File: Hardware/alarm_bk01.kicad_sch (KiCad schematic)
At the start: 18 parts, among them Q1 2N3904, SW1 START, SW2 Sensor, SW3 SW_SPDT, U1 ATtiny85V-10P

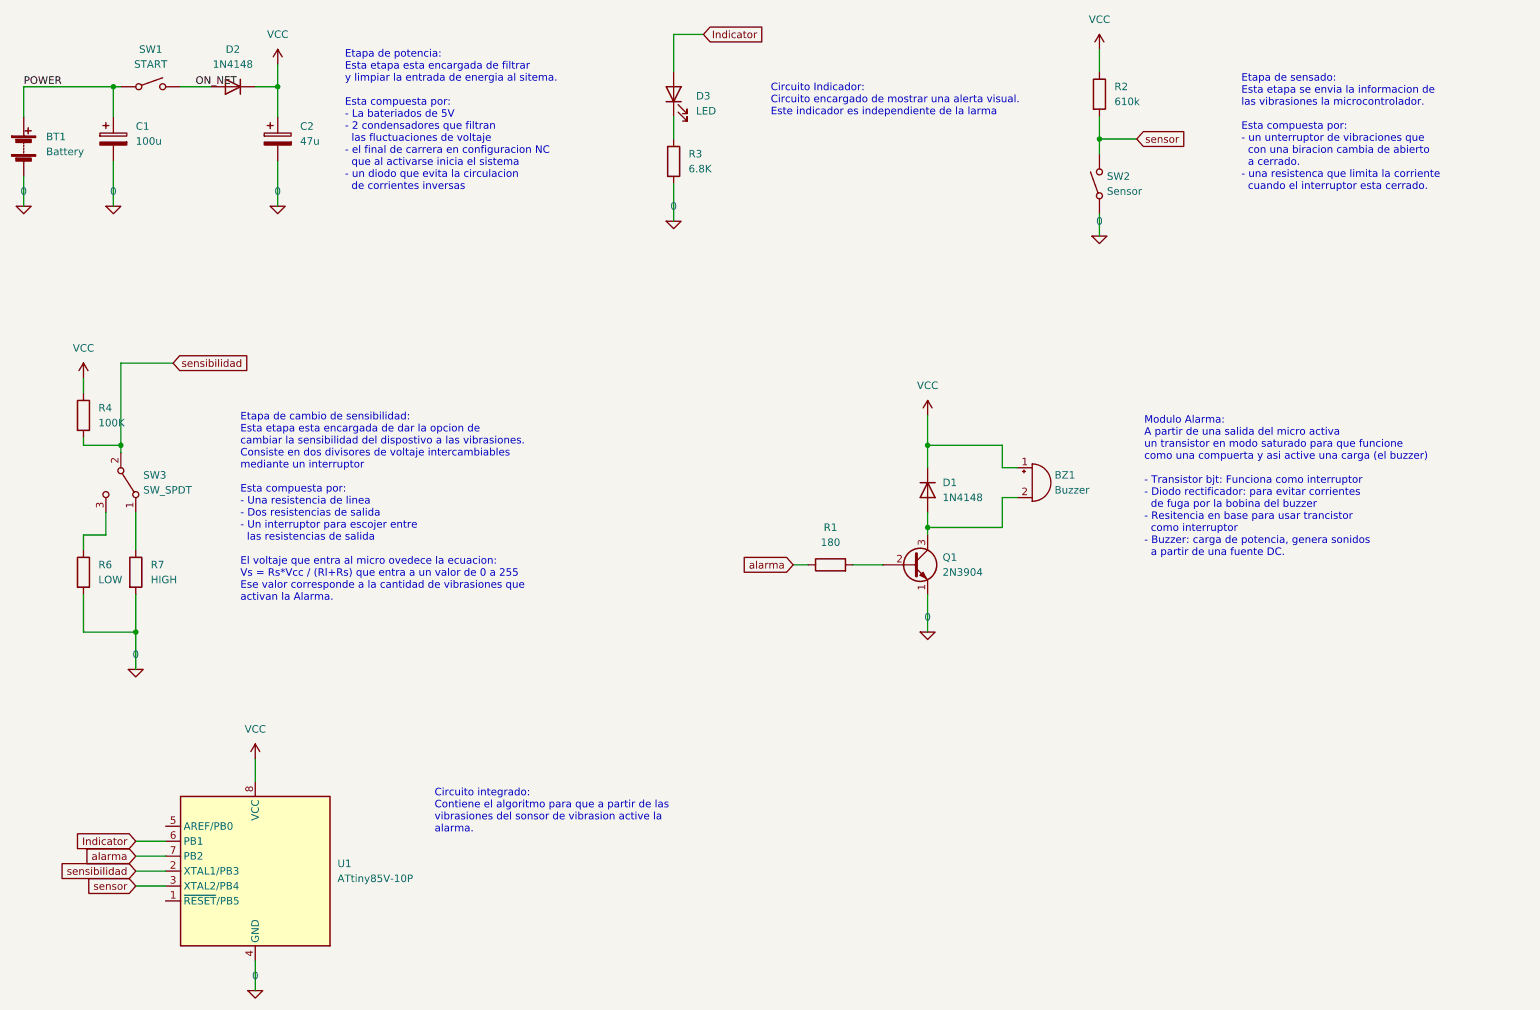
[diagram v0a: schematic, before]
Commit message: add smd design file
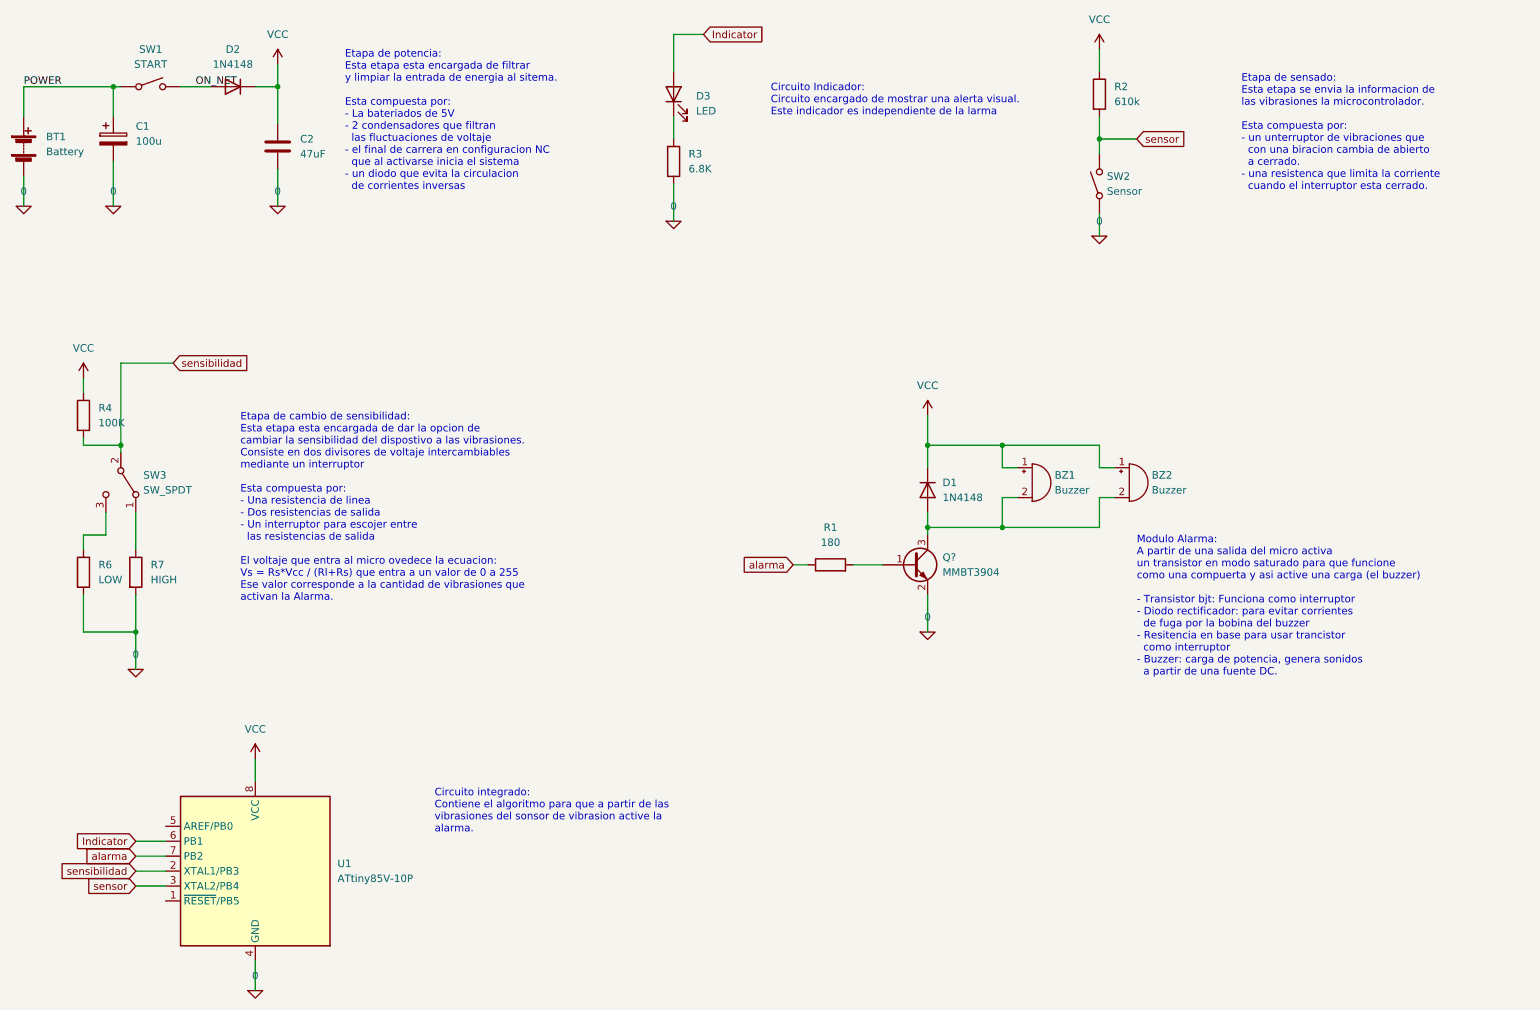
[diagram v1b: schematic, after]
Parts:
- removed C2: 47u, Capacitor_THT:CP_Radial_D5.0mm_P2.00mm, symbol Device:C_Polarized
- removed Q1: 2N3904, custom:TO-92_with_space, symbol Transistor_BJT:2N3904
- added BZ2: Buzzer, Connector_PinSocket_2.54mm:PinSocket_1x02_P2.54mm_Vertical_SMD_Pin1Left, symbol Device:Buzzer
- added C2: 47uF, Capacitor_SMD:C_0805_2012Metric, symbol Device:C
- added Q?: MMBT3904, Package_TO_SOT_SMD:SOT-23, symbol Transistor_BJT:MMBT3904
- BT1, BZ1: footprint Connector_JST:JST_EH_B2B-EH-A_1x02_P2.50mm_Vertical -> Connector_PinSocket_2.54mm:PinSocket_1x02_P2.54mm_Vertical_SMD_Pin1Left
- C1: footprint Capacitor_THT:CP_Radial_D5.0mm_P2.00mm -> Capacitor_SMD:CP_Elec_6.3x5.4
- D1, D2: footprint Diode_THT:D_DO-35_SOD27_P7.62mm_Horizontal -> Diode_SMD:D_SOD-123
- D3: footprint LED_THT:LED_D3.0mm_Horizontal_O1.27mm_Z2.0mm -> LED_THT:LED_D3.0mm_Horizontal_O3.81mm_Z2.0mm
- R1, R2, R3, R4, R6, R7: footprint Resistor_THT:R_Axial_DIN0207_L6.3mm_D2.5mm_P7.62mm_Horizontal -> Resistor_SMD:R_1206_3216Metric
- U1: footprint Package_DIP:DIP-8_W7.62mm -> Package_SO:SOP-8_3.9x4.9mm_P1.27mm
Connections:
- net 0: now also C2.2, Q?.2 (E)
- net VCC: now also BZ2.1 (-), C2.1
- net at BZ1.2 (+), D1.2 (A): now also BZ2.2 (+), Q?.3 (C)
- net at R1.2: now also Q?.1 (B)

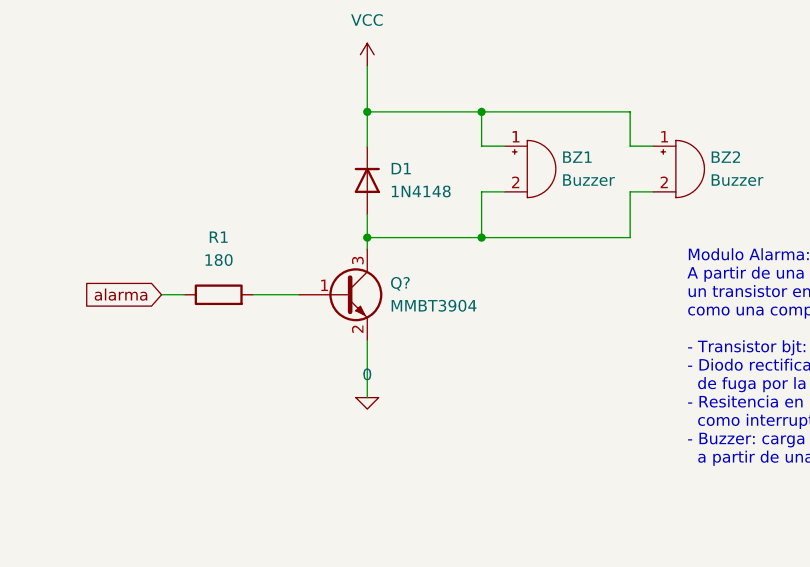
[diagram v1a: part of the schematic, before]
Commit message: pcb and holes of the new model
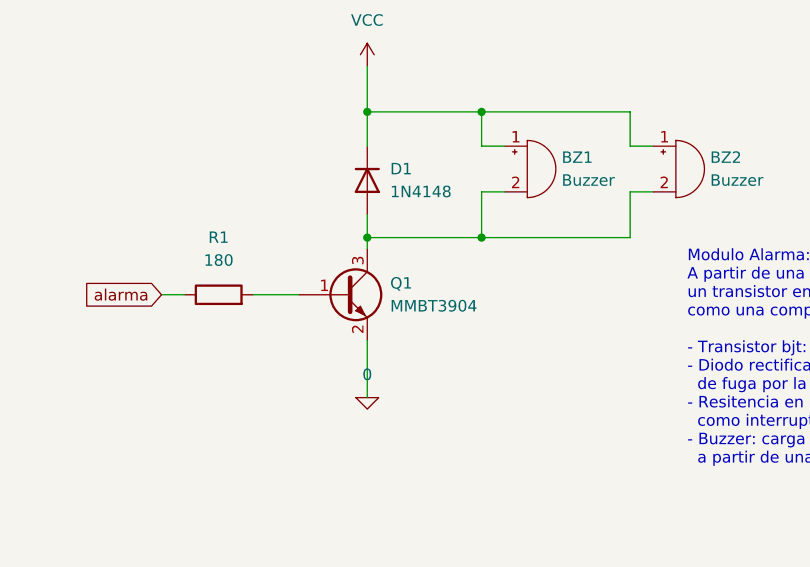
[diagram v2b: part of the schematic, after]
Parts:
- BZ1, BZ2: footprint Connector_PinSocket_2.54mm:PinSocket_1x02_P2.54mm_Vertical_SMD_Pin1Left -> Buzzer_Beeper:Buzzer_12x9.5RM7.6
- gave numbers to parts that had none: 1
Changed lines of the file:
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@@
   (symbol (lib_id "Transistor_BJT:MMBT3904") (at 181.61 114.3 0) (unit 1)
     (in_bom yes) (on_board yes) (fields_autoplaced)
-    (property "Reference" "Q?" (id 0) (at 186.69 113.0299 0)
+    (property "Reference" "Q1" (id 0) (at 186.69 113.0299 0)
       (effects (font (size 1.27 1.27)) (justify left))
     )
@@
       (effects (font (size 1.27 1.27)) (justify left))
     )
-    (property "Footprint" "Connector_PinSocket_2.54mm:PinSocket_1x02_P2.54mm_Vertical_SMD_Pin1Left" (id 2) (at 201.295 97.79 90)
+    (property "Footprint" "Buzzer_Beeper:Buzzer_12x9.5RM7.6" (id 2) (at 201.295 97.79 90)
       (effects (font (size 1.27 1.27)) hide)
     )
@@
       (effects (font (size 1.27 1.27)) (justify left))
     )
-    (property "Footprint" "Connector_PinSocket_2.54mm:PinSocket_1x02_P2.54mm_Vertical_SMD_Pin1Left" (id 2) (at 217.805 97.79 90)
+    (property "Footprint" "Buzzer_Beeper:Buzzer_12x9.5RM7.6" (id 2) (at 217.805 97.79 90)
       (effects (font (size 1.27 1.27)) hide)
     )
@@
     )
     (path "/62b1c3a5-5b3d-41c0-87bf-3745073e4764"
-      (reference "BZ1") (unit 1) (value "Buzzer") (footprint "Connector_PinSocket_2.54mm:PinSocket_1x02_P2.54mm_Vertical_SMD_Pin1Left")
+      (reference "BZ1") (unit 1) (value "Buzzer") (footprint "Buzzer_Beeper:Buzzer_12x9.5RM7.6")
     )
     (path "/d055d058-4a7f-4fe6-bc16-72f2dd4caaad"
-      (reference "BZ2") (unit 1) (value "Buzzer") (footprint "Connector_PinSocket_2.54mm:PinSocket_1x02_P2.54mm_Vertical_SMD_Pin1Left")
+      (reference "BZ2") (unit 1) (value "Buzzer") (footprint "Buzzer_Beeper:Buzzer_12x9.5RM7.6")
     )
     (path "/f9d78065-9a5e-4d58-b424-72b0930f1c67"
@@
     )
     (path "/44c6629f-444c-4570-ae20-d18b013e1452"
-      (reference "Q?") (unit 1) (value "MMBT3904") (footprint "Package_TO_SOT_SMD:SOT-23")
+      (reference "Q1") (unit 1) (value "MMBT3904") (footprint "Package_TO_SOT_SMD:SOT-23")
     )
     (path "/9d7bf49a-8ec5-4160-a5bc-4a0fd8b49fa5"

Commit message: Finish smd board
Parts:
- BT1: footprint Connector_PinSocket_2.54mm:PinSocket_1x02_P2.54mm_Vertical_SMD_Pin1Left -> Connector_JST:JST_XH_B2B-XH-A_1x02_P2.50mm_Vertical
- SW2: footprint custom:WS420 -> custom:CX-2548
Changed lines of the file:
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@@
       (effects (font (size 1.27 1.27)) (justify right))
     )
-    (property "Footprint" "custom:WS420" (id 2) (at 208.28 49.53 0)
+    (property "Footprint" "custom:CX-2548" (id 2) (at 208.28 49.53 0)
       (effects (font (size 1.27 1.27)) hide)
     )
@@
       (effects (font (size 1.27 1.27)) (justify left))
     )
-    (property "Footprint" "Connector_PinSocket_2.54mm:PinSocket_1x02_P2.54mm_Vertical_SMD_Pin1Left" (id 2) (at 30.48 41.656 90)
+    (property "Footprint" "Connector_JST:JST_XH_B2B-XH-A_1x02_P2.50mm_Vertical" (id 2) (at 30.48 41.656 90)
       (effects (font (size 1.27 1.27)) hide)
     )
@@
     )
     (path "/a1ff142e-222a-487e-ab42-3d9925a354a7"
-      (reference "BT1") (unit 1) (value "Battery") (footprint "Connector_PinSocket_2.54mm:PinSocket_1x02_P2.54mm_Vertical_SMD_Pin1Left")
+      (reference "BT1") (unit 1) (value "Battery") (footprint "Connector_JST:JST_XH_B2B-XH-A_1x02_P2.50mm_Vertical")
     )
     (path "/62b1c3a5-5b3d-41c0-87bf-3745073e4764"
@@
     )
     (path "/8af485cd-02c4-4345-a1c0-5f4c331e670b"
-      (reference "SW2") (unit 1) (value "Sensor") (footprint "custom:WS420")
+      (reference "SW2") (unit 1) (value "Sensor") (footprint "custom:CX-2548")
     )
     (path "/27696774-af07-4965-b944-23123e757a25"

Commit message: last update
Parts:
- C1: footprint Capacitor_SMD:CP_Elec_6.3x5.4 -> Capacitor_THT:CP_Radial_D6.3mm_P2.50mm
- R2: value 610k -> 10k
- U1: footprint Package_SO:SOP-8_3.9x4.9mm_P1.27mm -> custom:SOIC127P798X216-8N
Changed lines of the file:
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@@
       (effects (font (size 1.27 1.27)) (justify right))
     )
-    (property "Footprint" "Package_SO:SOP-8_3.9x4.9mm_P1.27mm" (id 2) (at 69.85 166.37 0)
+    (property "Footprint" "custom:SOIC127P798X216-8N" (id 2) (at 69.85 166.37 0)
       (effects (font (size 1.27 1.27) italic) hide)
     )
@@
       (effects (font (size 1.27 1.27)) (justify left))
     )
-    (property "Value" "610k" (id 1) (at 215.9 35.5599 0)
+    (property "Value" "10k" (id 1) (at 215.9 35.5599 0)
       (effects (font (size 1.27 1.27)) (justify left))
     )
@@
       (effects (font (size 1.27 1.27)) (justify left))
     )
-    (property "Footprint" "Capacitor_SMD:CP_Elec_6.3x5.4" (id 2) (at 46.6852 45.72 0)
+    (property "Footprint" "Capacitor_THT:CP_Radial_D6.3mm_P2.50mm" (id 2) (at 46.6852 45.72 0)
       (effects (font (size 1.27 1.27)) hide)
     )
@@
     )
     (path "/f9d78065-9a5e-4d58-b424-72b0930f1c67"
-      (reference "C1") (unit 1) (value "100u") (footprint "Capacitor_SMD:CP_Elec_6.3x5.4")
+      (reference "C1") (unit 1) (value "100u") (footprint "Capacitor_THT:CP_Radial_D6.3mm_P2.50mm")
     )
     (path "/b9c60bfc-e42e-4b48-a6c6-ec86acdc075f"
@@
     )
     (path "/e9302728-fab8-4758-8a1e-cae903553c53"
-      (reference "R2") (unit 1) (value "610k") (footprint "Resistor_SMD:R_1206_3216Metric")
+      (reference "R2") (unit 1) (value "10k") (footprint "Resistor_SMD:R_1206_3216Metric")
     )
     (path "/f9ee9165-8fac-4d3d-ae5a-9f696219d2e8"
@@
     )
     (path "/da5ed42c-756f-4c9b-902f-2bd2562efcb7"
-      (reference "U1") (unit 1) (value "ATtiny85V-10P") (footprint "Package_SO:SOP-8_3.9x4.9mm_P1.27mm")
-    )
-  )
+      (reference "U1") (unit 1) (value "ATtiny85V-10P") (footprint "custom:SOIC127P798X216-8N")
+    )
+  )
